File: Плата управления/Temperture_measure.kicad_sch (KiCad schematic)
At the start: 14 parts, among them U8 LMV324

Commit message: Привел в порядок схему
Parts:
- renumbered C18 to C15, C19 to C16, C20 to C17, R22 to R24, R23 to R25, R27 to R26, U8 to U3
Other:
- note added: "Питание"
- note added: "Температура А"
- note added: "Температура В"
- note added: "Температура С"
- moved on the sheet: C14, C15, C16, C17, R24, R25, R26, U3A, U3B, U3C, U3E

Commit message: Расставил компоненты по плате
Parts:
- R24, R25, R26: footprint Resistor_SMD:R_0805_2012Metric_Pad1.20x1.40mm_HandSolder -> Resistor_SMD:R_0603_1608Metric_Pad0.98x0.95mm_HandSolder
- U3: footprint (none) -> Package_SO:SOIC-14_3.9x8.7mm_P1.27mm
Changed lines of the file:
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@@
       (effects (font (size 1.27 1.27)))
     )
-    (property "Footprint" "" (at 77.47 135.89 0)
+    (property "Footprint" "Package_SO:SOIC-14_3.9x8.7mm_P1.27mm" (at 77.47 135.89 0)
       (effects (font (size 1.27 1.27)) hide)
     )
@@
       (effects (font (size 1.27 1.27)))
     )
-    (property "Footprint" "" (at 76.2 87.63 0)
+    (property "Footprint" "Package_SO:SOIC-14_3.9x8.7mm_P1.27mm" (at 76.2 87.63 0)
       (effects (font (size 1.27 1.27)) hide)
     )
@@
       (effects (font (size 1.27 1.27)) (justify left))
     )
-    (property "Footprint" "" (at 135.89 35.56 0)
+    (property "Footprint" "Package_SO:SOIC-14_3.9x8.7mm_P1.27mm" (at 135.89 35.56 0)
       (effects (font (size 1.27 1.27)) hide)
     )
@@
       (effects (font (size 1.27 1.27)))
     )
-    (property "Footprint" "" (at 77.47 39.37 0)
+    (property "Footprint" "Package_SO:SOIC-14_3.9x8.7mm_P1.27mm" (at 77.47 39.37 0)
       (effects (font (size 1.27 1.27)) hide)
     )
@@
       (effects (font (size 1.27 1.27)) (justify left))
     )
-    (property "Footprint" "Resistor_SMD:R_0805_2012Metric_Pad1.20x1.40mm_HandSolder" (at 41.402 81.28 90)
+    (property "Footprint" "Resistor_SMD:R_0603_1608Metric_Pad0.98x0.95mm_HandSolder" (at 41.402 81.28 90)
       (effects (font (size 1.27 1.27)) hide)
     )
@@
       (effects (font (size 1.27 1.27)) (justify left))
     )
-    (property "Footprint" "Resistor_SMD:R_0805_2012Metric_Pad1.20x1.40mm_HandSolder" (at 42.672 33.02 90)
+    (property "Footprint" "Resistor_SMD:R_0603_1608Metric_Pad0.98x0.95mm_HandSolder" (at 42.672 33.02 90)
       (effects (font (size 1.27 1.27)) hide)
     )
@@
       (effects (font (size 1.27 1.27)) (justify left))
     )
-    (property "Footprint" "Resistor_SMD:R_0805_2012Metric_Pad1.20x1.40mm_HandSolder" (at 42.672 129.54 90)
-      (effects (font (size 1.27 1.27)) hide)
-    )
+    (property "Footprint" "Resistor_SMD:R_0603_1608Metric_Pad0.98x0.95mm_HandSolder" (at 42.672 129.54 90)
+      (effects (font (size 1.27 1.27)) hide)
+    )

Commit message: Новый контур платы
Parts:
- added C20, C60, C61: 56p, Capacitor_SMD:C_0603_1608Metric_Pad1.08x0.95mm_HandSolder, symbol Device:C_Small
- added R39, R40, R41: 120, Resistor_SMD:R_0603_1608Metric_Pad0.98x0.95mm_HandSolder, symbol Device:R_Small
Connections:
- net GND: now also C20.2, C60.2, C61.2
- new net Temp_Coil1: R41.1
- new net Temp_Coil1_MCU: C61.1, R41.2
- new net Temp_Coil2: R39.1
- new net Temp_Coil2_MCU: C20.1, R39.2
- new net Temp_Coil3: R40.1
- new net Temp_Coil3_MCU: C60.1, R40.2
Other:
- note added: "Температура обмотки 1"
- note added: "Температура обмотки 2"
- note added: "Температура обмотки 3"
- moved on the sheet: C14, U3E

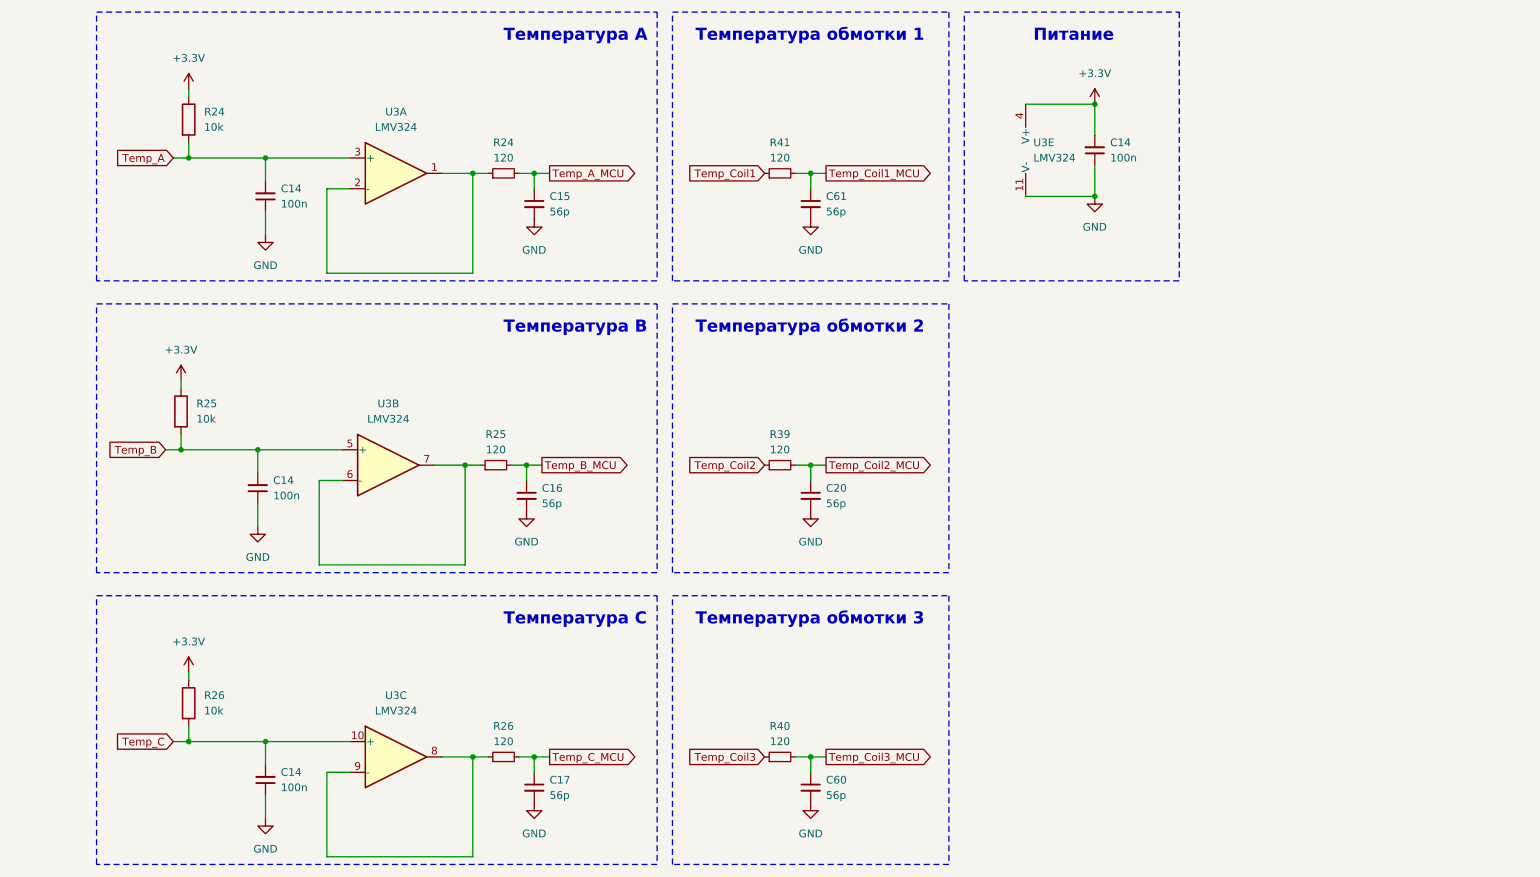
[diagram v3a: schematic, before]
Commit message: Заменил разъём под силовую плату
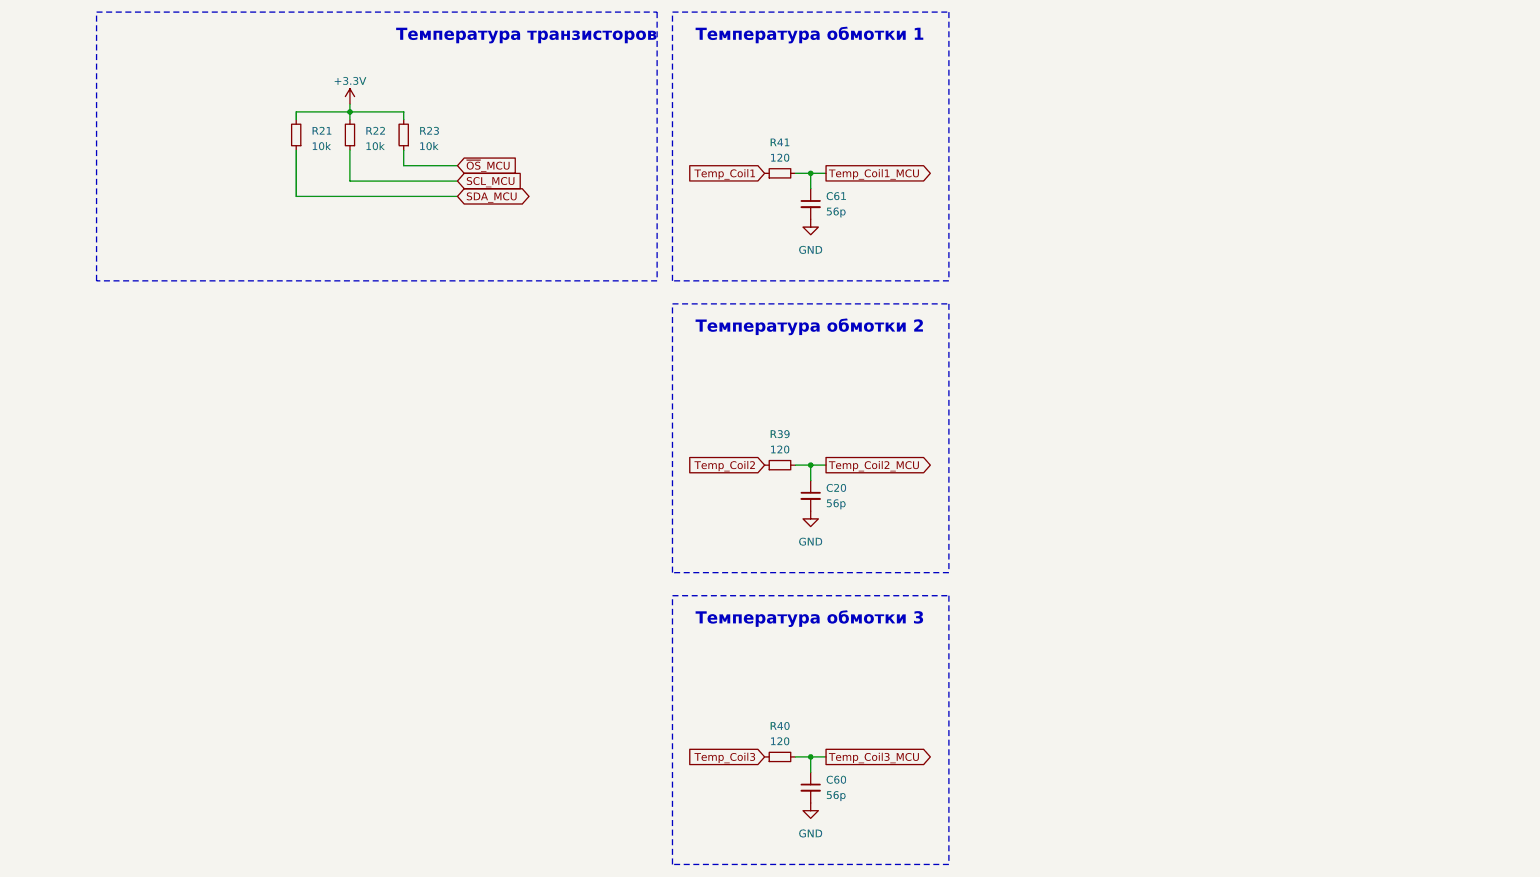
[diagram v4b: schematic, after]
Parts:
- removed C14 (x4): 100n, Capacitor_SMD:C_0603_1608Metric_Pad1.08x0.95mm_HandSolder, symbol Device:C_Small
- removed C15, C16, C17: 56p, Capacitor_SMD:C_0603_1608Metric_Pad1.08x0.95mm_HandSolder, symbol Device:C_Small
- removed R24, R25, R26: 120, Resistor_SMD:R_0603_1608Metric_Pad0.98x0.95mm_HandSolder, symbol Device:R_Small
- removed R24, R25, R26: 10k, Resistor_SMD:R_0603_1608Metric_Pad0.98x0.95mm_HandSolder, symbol Device:R
- removed U3: LMV324, Package_SO:SOIC-14_3.9x8.7mm_P1.27mm, symbol Amplifier_Operational:LMV324
- added R21, R22, R23: 10k, Resistor_SMD:R_0603_1608Metric_Pad0.98x0.95mm_HandSolder, symbol Device:R_Small
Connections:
- net +3.3V: now also R21.2, R22.2, R23.2
- new net SCL_MCU: R22.1
- new net SDA_MCU: R21.1
- new net ~{OS}_MCU: R23.1
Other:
- note added: "Температура транзисторов"
- note removed: "Питание"
- note removed: "Температура А"
- note removed: "Температура В"
- note removed: "Температура С"

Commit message: Разделил аналоговое и цифровое питание
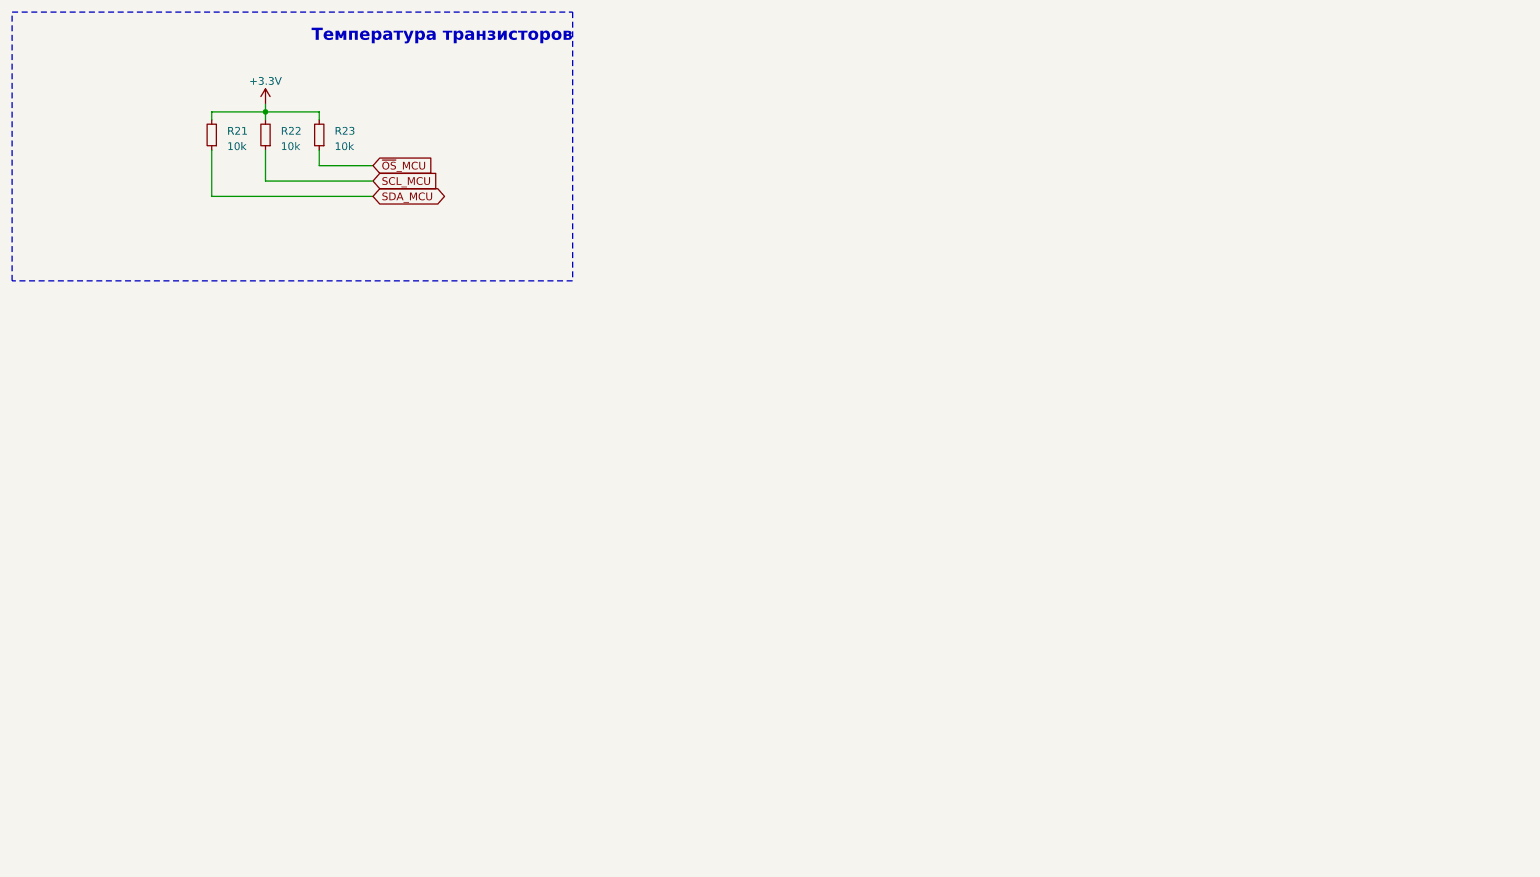
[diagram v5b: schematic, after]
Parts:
- removed C20, C60, C61: 56p, Capacitor_SMD:C_0603_1608Metric_Pad1.08x0.95mm_HandSolder, symbol Device:C_Small
- removed R39, R40, R41: 120, Resistor_SMD:R_0603_1608Metric_Pad0.98x0.95mm_HandSolder, symbol Device:R_Small
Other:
- note removed: "Температура обмотки 1"
- note removed: "Температура обмотки 2"
- note removed: "Температура обмотки 3"
- moved on the sheet: R21, R22, R23

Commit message: Редактировал схему
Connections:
- net SCL_MCU renamed Temperature_Power_SCL_MCU
- net SDA_MCU renamed Temperature_Power_SDA_MCU
- net ~{OS}_MCU renamed Temperature_Power_~{OS}_MCU
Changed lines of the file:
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@@
     (effects (font (size 2 2) bold) (justify left bottom))
   )
-  (global_label "SDA_MCU" (shape bidirectional) (at 74.93 45.72 0) (fields_autoplaced)
+  (global_label "Temperature_Power_SDA_MCU" (shape bidirectional) (at 74.93 45.72 0) (fields_autoplaced)
     (effects (font (size 1.27 1.27)) (justify left))
-    (property "Intersheetrefs" "${INTERSHEET_REFS}" (at 87.5347 45.72 0)
+    (property "Intersheetrefs" "${INTERSHEET_REFS}" (at 106.8454 45.72 0)
       (effects (font (size 1.27 1.27)) (justify left) hide)
     )
   )
-  (global_label "SCL_MCU" (shape input) (at 74.93 43.18 0) (fields_autoplaced)
+  (global_label "Temperature_Power_SCL_MCU" (shape input) (at 74.93 43.18 0) (fields_autoplaced)
     (effects (font (size 1.27 1.27)) (justify left))
-    (property "Intersheetrefs" "${INTERSHEET_REFS}" (at 86.3629 43.18 0)
+    (property "Intersheetrefs" "${INTERSHEET_REFS}" (at 105.6736 43.18 0)
       (effects (font (size 1.27 1.27)) (justify left) hide)
     )
   )
-  (global_label "~{OS}_MCU" (shape input) (at 74.93 40.64 0) (fields_autoplaced)
+  (global_label "Temperature_Power_~{OS}_MCU" (shape input) (at 74.93 40.64 0) (fields_autoplaced)
     (effects (font (size 1.27 1.27)) (justify left))
-    (property "Intersheetrefs" "${INTERSHEET_REFS}" (at 85.3953 40.64 0)
+    (property "Intersheetrefs" "${INTERSHEET_REFS}" (at 104.706 40.64 0)
       (effects (font (size 1.27 1.27)) (justify left) hide)
     )

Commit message: Добавил документы
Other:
- moved on the sheet: R21, R22, R23
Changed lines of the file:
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@@
 (kicad_sch (version 20230121) (generator eeschema)
   (paper "A4")
-  (junction (at 57.15 31.75) (diameter 0) (color 0 0 0 0)
+  (title_block
+    (comment 1 "МПСТ.76721.758764.02.Э3.М")
   )
-  (wire (pts (xy 74.93 45.72) (xy 48.26 45.72))
+  (junction (at 139.7 93.345) (diameter 0) (color 0 0 0 0)
+  )
+  (wire (pts (xy 157.48 107.315) (xy 130.81 107.315))
     (stroke (width 0) (type default))
   )
-  (wire (pts (xy 74.93 40.64) (xy 66.04 40.64))
+  (wire (pts (xy 157.48 102.235) (xy 148.59 102.235))
     (stroke (width 0) (type default))
   )
-  (wire (pts (xy 57.15 31.75) (xy 57.15 33.02))
+  (wire (pts (xy 139.7 93.345) (xy 139.7 94.615))
     (stroke (width 0) (type default))
   )
-  (wire (pts (xy 57.15 30.48) (xy 57.15 31.75))
+  (wire (pts (xy 139.7 92.075) (xy 139.7 93.345))
     (stroke (width 0) (type default))
   )
-  (wire (pts (xy 57.15 43.18) (xy 57.15 38.1))
+  (wire (pts (xy 139.7 104.775) (xy 139.7 99.695))
     (stroke (width 0) (type default))
   )
-  (wire (pts (xy 66.04 33.02) (xy 66.04 31.75))
+  (wire (pts (xy 148.59 94.615) (xy 148.59 93.345))
     (stroke (width 0) (type default))
   )
-  (wire (pts (xy 66.04 40.64) (xy 66.04 38.1))
+  (wire (pts (xy 148.59 102.235) (xy 148.59 99.695))
     (stroke (width 0) (type default))
   )
-  (wire (pts (xy 48.26 31.75) (xy 57.15 31.75))
+  (wire (pts (xy 130.81 93.345) (xy 139.7 93.345))
     (stroke (width 0) (type default))
   )
-  (wire (pts (xy 57.15 31.75) (xy 66.04 31.75))
+  (wire (pts (xy 139.7 93.345) (xy 148.59 93.345))
     (stroke (width 0) (type default))
   )
-  (wire (pts (xy 48.26 33.02) (xy 48.26 31.75))
+  (wire (pts (xy 130.81 94.615) (xy 130.81 93.345))
     (stroke (width 0) (type default))
   )
-  (wire (pts (xy 48.26 45.72) (xy 48.26 38.1))
+  (wire (pts (xy 130.81 107.315) (xy 130.81 99.695))
     (stroke (width 0) (type default))
   )
-  (wire (pts (xy 74.93 43.18) (xy 57.15 43.18))
+  (wire (pts (xy 157.48 104.775) (xy 139.7 104.775))
     (stroke (width 0) (type default))
   )
-  (rectangle (start 15.24 15.24) (end 107.95 59.69)
-    (stroke (width 0) (type dot))
+  (rectangle (start 125.095 76.835) (end 190.5 121.285)
+    (stroke (width 0) (type dash))
     (fill (type none))
   )
-  (text "Температура транзисторов" (at 64.77 20.32 0)
+  (text "Температура транзисторов" (at 137.795 76.2 0)
     (effects (font (size 2 2) bold) (justify left bottom))
   )
-  (global_label "Temperature_Power_SDA_MCU" (shape bidirectional) (at 74.93 45.72 0) (fields_autoplaced)
+  (global_label "Temperature_Power_SDA_MCU" (shape bidirectional) (at 157.48 107.315 0) (fields_autoplaced)
     (effects (font (size 1.27 1.27)) (justify left))
-    (property "Intersheetrefs" "${INTERSHEET_REFS}" (at 106.8454 45.72 0)
+    (property "Intersheetrefs" "${INTERSHEET_REFS}" (at 189.3954 107.315 0)
       (effects (font (size 1.27 1.27)) (justify left) hide)
     )
   )
-  (global_label "Temperature_Power_SCL_MCU" (shape input) (at 74.93 43.18 0) (fields_autoplaced)
+  (global_label "Temperature_Power_SCL_MCU" (shape input) (at 157.48 104.775 0) (fields_autoplaced)
     (effects (font (size 1.27 1.27)) (justify left))
-    (property "Intersheetrefs" "${INTERSHEET_REFS}" (at 105.6736 43.18 0)
+    (property "Intersheetrefs" "${INTERSHEET_REFS}" (at 188.2236 104.775 0)
       (effects (font (size 1.27 1.27)) (justify left) hide)
     )
   )
-  (global_label "Temperature_Power_~{OS}_MCU" (shape input) (at 74.93 40.64 0) (fields_autoplaced)
+  (global_label "Temperature_Power_~{OS}_MCU" (shape input) (at 157.48 102.235 0) (fields_autoplaced)
     (effects (font (size 1.27 1.27)) (justify left))
-    (property "Intersheetrefs" "${INTERSHEET_REFS}" (at 104.706 40.64 0)
+    (property "Intersheetrefs" "${INTERSHEET_REFS}" (at 187.256 102.235 0)
       (effects (font (size 1.27 1.27)) (justify left) hide)
     )
   )
-  (symbol (lib_id "Device:R_Small") (at 66.04 35.56 180) (unit 1)
+  (symbol (lib_id "Device:R_Small") (at 148.59 97.155 180) (unit 1)
     (in_bom yes) (on_board yes) (dnp no) (fields_autoplaced)
-    (property "Reference" "R23" (at 68.58 34.925 0)
+    (property "Reference" "R23" (at 151.13 96.52 0)
       (effects (font (size 1.27 1.27)) (justify right))
     )
-    (property "Value" "10k" (at 68.58 37.465 0)
+    (property "Value" "10k" (at 151.13 99.06 0)
       (effects (font (size 1.27 1.27)) (justify right))
     )
-    (property "Footprint" "Resistor_SMD:R_0603_1608Metric_Pad0.98x0.95mm_HandSolder" (at 66.04 35.56 0)
+    (property "Footprint" "Resistor_SMD:R_0603_1608Metric_Pad0.98x0.95mm_HandSolder" (at 148.59 97.155 0)
       (effects (font (size 1.27 1.27)) hide)
     )
-    (property "Datasheet" "~" (at 66.04 35.56 0)
+    (property "Datasheet" "~" (at 148.59 97.155 0)
       (effects (font (size 1.27 1.27)) hide)
     )
@@
     )
   )
-  (symbol (lib_id "power:+3.3V") (at 57.15 30.48 0) (unit 1)
+  (symbol (lib_id "power:+3.3V") (at 139.7 92.075 0) (unit 1)
     (in_bom yes) (on_board yes) (dnp no) (fields_autoplaced)
-    (property "Reference" "#PWR029" (at 57.15 34.29 0)
+    (property "Reference" "#PWR029" (at 139.7 95.885 0)
       (effects (font (size 1.27 1.27)) hide)
     )
-    (property "Value" "+3.3V" (at 57.15 26.67 0)
+    (property "Value" "+3.3V" (at 139.7 88.265 0)
       (effects (font (size 1.27 1.27)))
     )
-    (property "Footprint" "" (at 57.15 30.48 0)
+    (property "Footprint" "" (at 139.7 92.075 0)
       (effects (font (size 1.27 1.27)) hide)
     )
-    (property "Datasheet" "" (at 57.15 30.48 0)
+    (property "Datasheet" "" (at 139.7 92.075 0)
       (effects (font (size 1.27 1.27)) hide)
     )
@@
     )
   )
-  (symbol (lib_id "Device:R_Small") (at 48.26 35.56 180) (unit 1)
+  (symbol (lib_id "Device:R_Small") (at 130.81 97.155 180) (unit 1)
     (in_bom yes) (on_board yes) (dnp no) (fields_autoplaced)
-    (property "Reference" "R21" (at 50.8 34.925 0)
+    (property "Reference" "R21" (at 133.35 96.52 0)
       (effects (font (size 1.27 1.27)) (justify right))
     )
-    (property "Value" "10k" (at 50.8 37.465 0)
+    (property "Value" "10k" (at 133.35 99.06 0)
       (effects (font (size 1.27 1.27)) (justify right))
     )
-    (property "Footprint" "Resistor_SMD:R_0603_1608Metric_Pad0.98x0.95mm_HandSolder" (at 48.26 35.56 0)
+    (property "Footprint" "Resistor_SMD:R_0603_1608Metric_Pad0.98x0.95mm_HandSolder" (at 130.81 97.155 0)
       (effects (font (size 1.27 1.27)) hide)
     )
-    (property "Datasheet" "~" (at 48.26 35.56 0)
+    (property "Datasheet" "~" (at 130.81 97.155 0)
       (effects (font (size 1.27 1.27)) hide)
     )
@@
     )
   )
-  (symbol (lib_id "Device:R_Small") (at 57.15 35.56 180) (unit 1)
+  (symbol (lib_id "Device:R_Small") (at 139.7 97.155 180) (unit 1)
     (in_bom yes) (on_board yes) (dnp no) (fields_autoplaced)
-    (property "Reference" "R22" (at 59.69 34.925 0)
+    (property "Reference" "R22" (at 142.24 96.52 0)
       (effects (font (size 1.27 1.27)) (justify right))
     )
-    (property "Value" "10k" (at 59.69 37.465 0)
+    (property "Value" "10k" (at 142.24 99.06 0)
       (effects (font (size 1.27 1.27)) (justify right))
     )
-    (property "Footprint" "Resistor_SMD:R_0603_1608Metric_Pad0.98x0.95mm_HandSolder" (at 57.15 35.56 0)
+    (property "Footprint" "Resistor_SMD:R_0603_1608Metric_Pad0.98x0.95mm_HandSolder" (at 139.7 97.155 0)
       (effects (font (size 1.27 1.27)) hide)
     )
-    (property "Datasheet" "~" (at 57.15 35.56 0)
+    (property "Datasheet" "~" (at 139.7 97.155 0)
       (effects (font (size 1.27 1.27)) hide)
     )
